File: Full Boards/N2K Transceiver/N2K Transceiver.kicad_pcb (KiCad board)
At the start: 4 copper layers, 80 x 60 mm, 75 parts, among them J1 JTAG, SW1 SW_MEC_5G, SW2 SW_MEC_5G, SW3 SW_MEC_5G

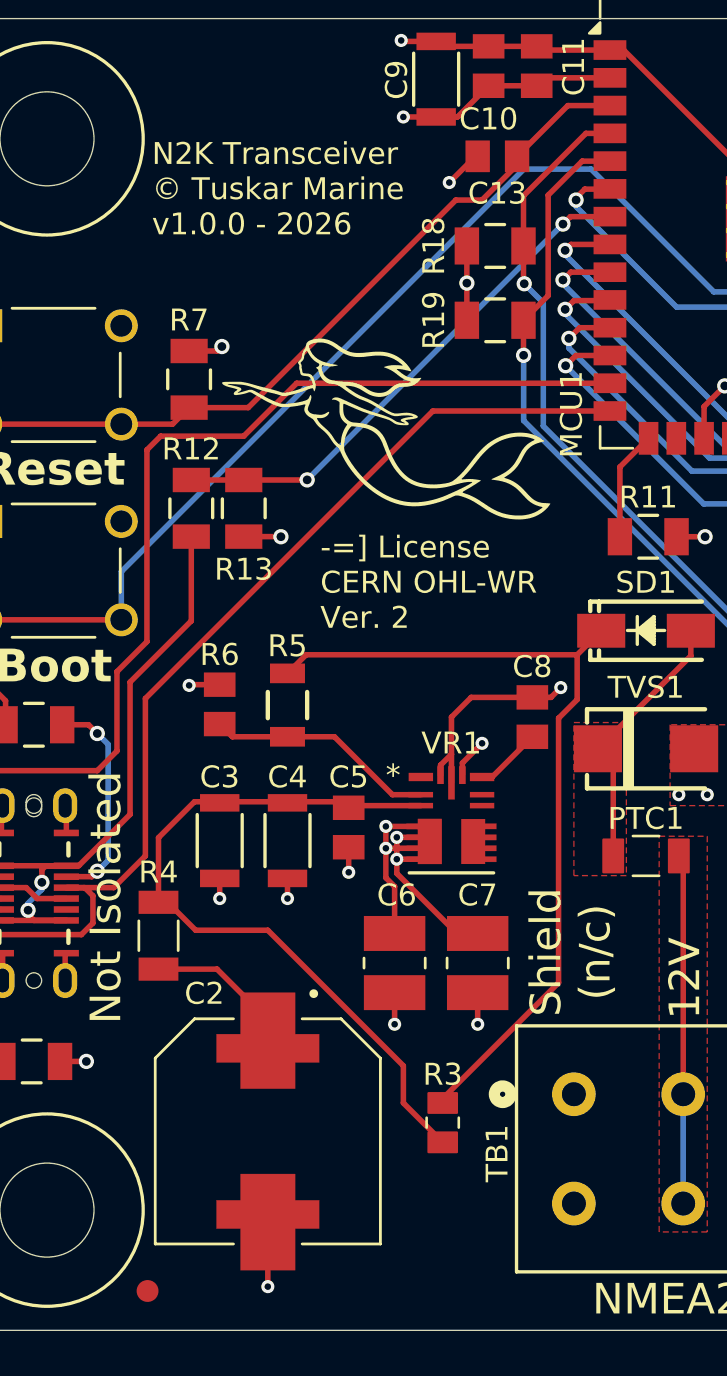
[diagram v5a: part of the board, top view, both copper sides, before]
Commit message: Removed the DNP'ed RC damper. With the TVS, it should not be possible for ringing to raise the voltage above 40v.
Signed-off-by: digimer <digital.mermaid@gmail.com>
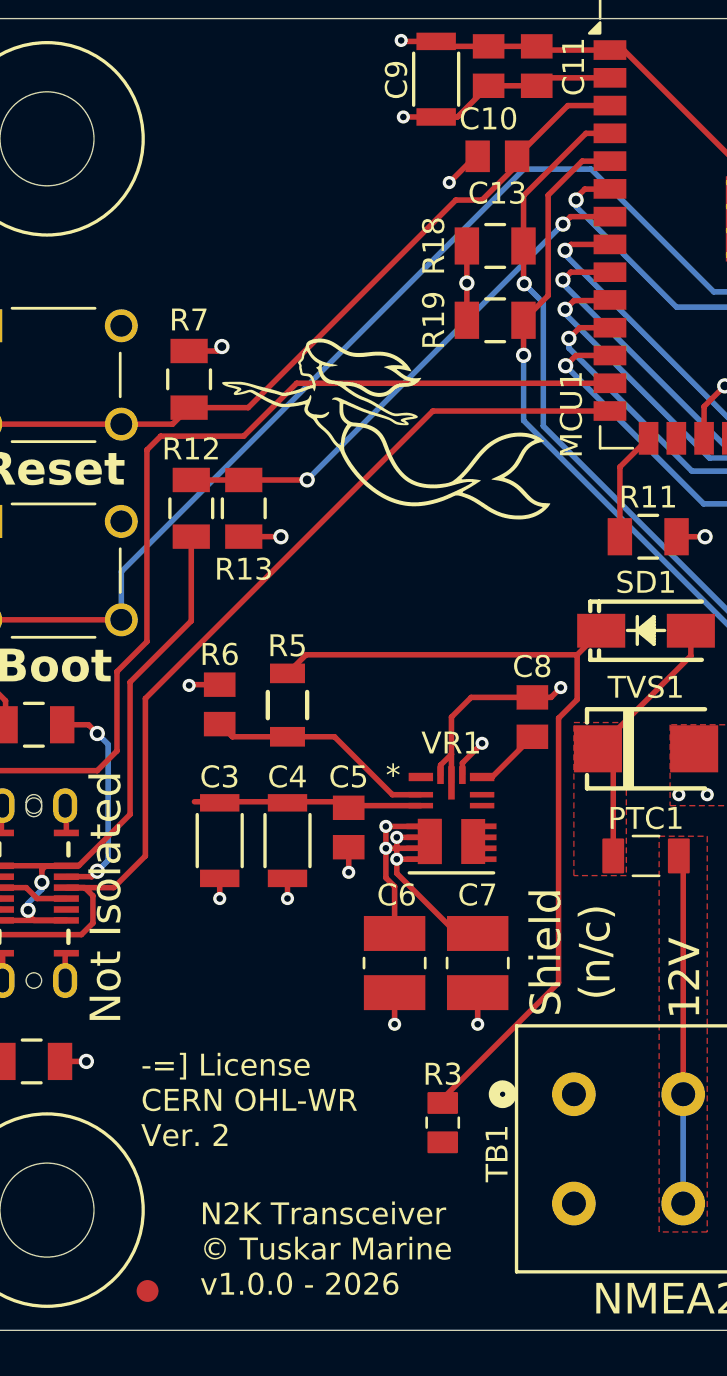
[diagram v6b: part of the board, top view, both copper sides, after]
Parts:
- removed C2: 330uF, mr-stuff:Panasonic EEH-ZU
- removed R4: 0.2R, mr-stuff:KOA SR73
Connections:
- C1 pad 2: GND -> +3.3V
- C10 pad 1: GND -> +3.3V
- C11 pad 1: GND -> +3.3V
- C14 pad 2: GND -> +3.3V
- C15 pad 2: GND -> +3.3V
- C6 pad 1: GND -> +3.3V
- C7 pad 1: GND -> +3.3V
- C9 pad 2: GND -> +3.3V
- CAN1 pad 3: GND -> +3.3V
- MCU1 pad 2: GND -> +3.3V
- R1 pad 2: GND -> +3.3V
- R16 pad 1: GND -> +3.3V
- R17 pad 1: GND -> +3.3V
- R18 pad 2: GND -> +3.3V
- R19 pad 2: GND -> +3.3V
- R23 pad 2: GND -> +3.3V
- R7 pad 2: GND -> +3.3V
- R8 pad 2: GND -> +3.3V
- ROM1 pad 1: GND -> +3.3V
- ROM1 pad 3: GND -> +3.3V
- ROM1 pad 8: GND -> +3.3V
- ROM2 pad 1: GND -> +3.3V
- ROM2 pad 2: GND -> +3.3V
- ROM2 pad 3: GND -> +3.3V
- ROM2 pad 8: GND -> +3.3V
- VR1 pad 4: GND -> +3.3V
- VR1 pad 9: GND -> +3.3V
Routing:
- net GND: track 214.5 -> 132.6 mm, vias 49 -> 32
- net +3.3V: track 0.00 -> 78.5 mm, vias 0 -> 16
- net Net-(VR1-VIN): track 33.5 -> 10.1 mm
- net Net-(C2-Pad1): track 7.26 -> 0.00 mm

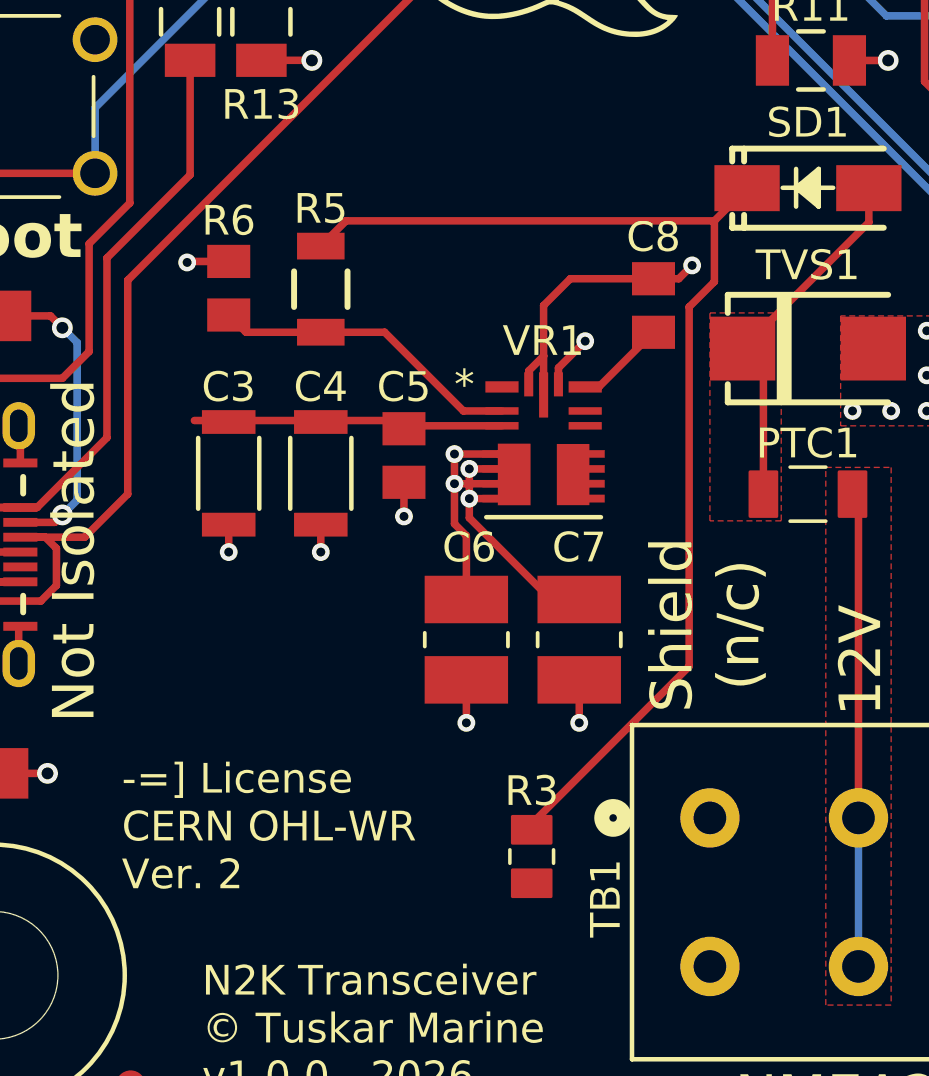
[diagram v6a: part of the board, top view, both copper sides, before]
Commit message: Resolved DRC issues.
Signed-off-by: digimer <digital.mermaid@gmail.com>
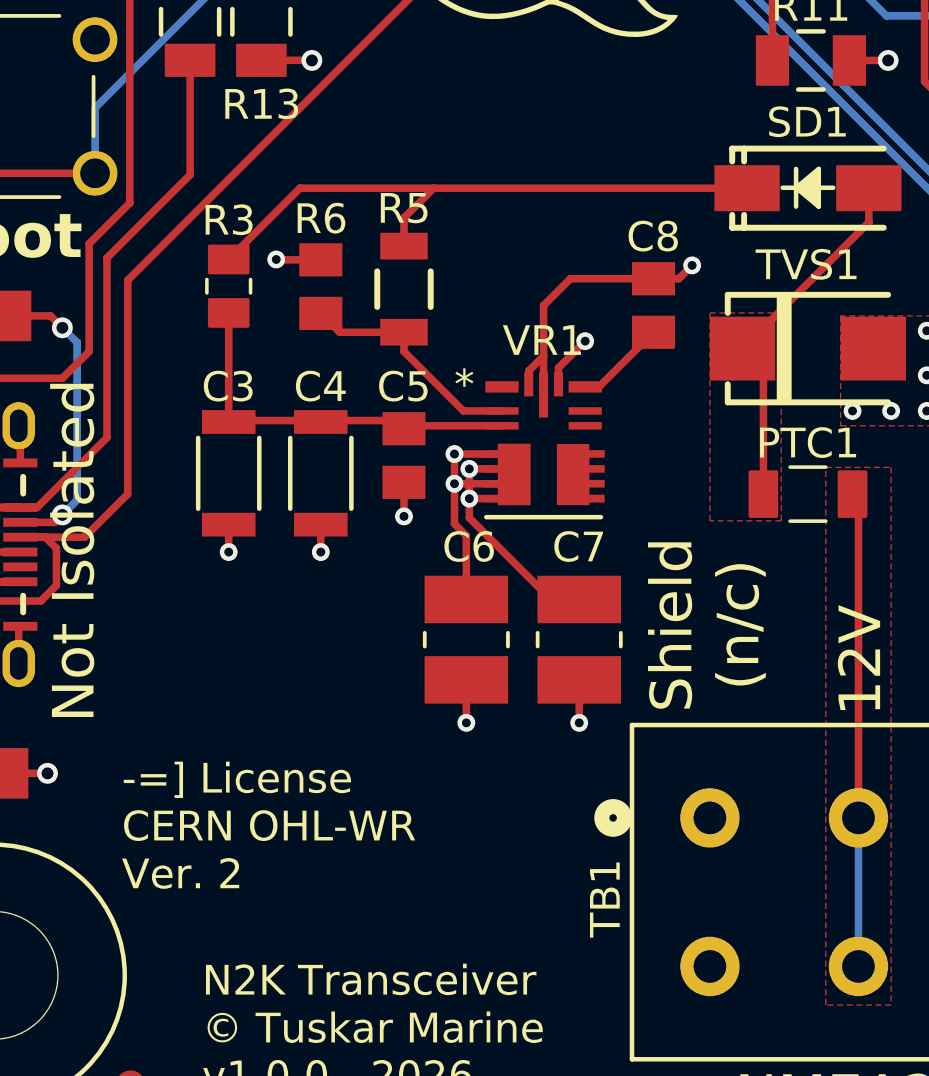
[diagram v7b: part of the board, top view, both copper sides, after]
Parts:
- moved R3 21.7 mm to (73.4, 74.6)
- moved R6 3.10 mm to (76.5, 74.6)
- moved R5 2.80 mm to (79.3, 74.7)
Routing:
- net V_RAW: track 38.0 -> 20.8 mm
- net Net-(VR1-EN): track 10.5 -> 7.84 mm
- net Net-(VR1-VIN): track 10.1 -> 12.6 mm
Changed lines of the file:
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@@
 	(footprint "mr-stuff:Vishay RCA-SR e3"
 		(layer "F.Cu")
-		(at 83.6 93.8 -90)
+		(at 73.4 74.6 -90)
 		(descr "Resistor SMD 0805")
 		(tags "resistor")
 		(property "Reference" "R3"
-			(at -2.2 0 180)
+			(at -2.2 0 0)
 			(layer "F.SilkS")
 			(effects
@@
 	(footprint "mr-stuff:Wurth WRIS-RSKS"
 		(layer "F.Cu")
-		(at 76.5 74.7 90)
+		(at 79.3 74.7 90)
 		(property "Reference" "R5"
 			(at 2.7 0 180)
@@
 	(footprint "mr-stuff:Stackpole RMCA0805"
 		(layer "F.Cu")
-		(at 73.4 74.6537 90)
+		(at 76.5 74.6 90)
 		(property "Reference" "R6"
 			(at 2.2537 0 0)
@@
 			(polygon
 				(pts
-					(xy 72.7269 74.9603) (xy 72.7269 74.3761) (xy 74.0731 74.3761) (xy 74.0731 74.9603)
+					(xy 75.8269 74.9066) (xy 75.8269 74.3224) (xy 77.1731 74.3224) (xy 77.1731 74.9066)
 				)
 			)
@@
 	)
 	(segment
-		(start 88.9 75.3)
-		(end 88.9 87.4)
-		(width 0.254)
-		(layer "F.Cu")
-		(net "V_RAW")
-	)
-	(segment
-		(start 89.75 72.4)
+		(start 80.3 71.3)
 		(end 90.85 71.3)
 		(width 0.254)
@@
 	)
 	(segment
-		(start 76.5 73.25)
-		(end 77.35 72.4)
-		(width 0.254)
-		(layer "F.Cu")
-		(net "V_RAW")
-	)
-	(segment
-		(start 89.75 72.4)
-		(end 89.75 74.45)
+		(start 79.3 73.25)
+		(end 79.3 72.3)
 		(width 0.254)
 		(layer "F.Cu")
@@
 	)
 	(segment
-		(start 77.35 72.4)
-		(end 89.75 72.4)
+		(start 73.4 73.7)
+		(end 75.8 71.3)
 		(width 0.254)
 		(layer "F.Cu")
@@
 	)
 	(segment
-		(start 89.75 74.45)
-		(end 88.9 75.3)
+		(start 79.3 72.3)
+		(end 80.3 71.3)
 		(width 0.254)
 		(layer "F.Cu")
@@
 	)
 	(segment
-		(start 88.9 87.4)
-		(end 83.6 92.7)
+		(start 75.8 71.3)
+		(end 80.3 71.3)
 		(width 0.254)
 		(layer "F.Cu")
@@
 	)
 	(segment
-		(start 72.2443 79.122)
-		(end 73.4 79.122)
+		(start 76.5 79.122)
+		(end 79.0737 79.122)
 		(width 0.254)
 		(layer "F.Cu")
@@
 	)
 	(segment
-		(start 76.5 79.122)
-		(end 79.0737 79.122)
+		(start 73.4 79.172)
+		(end 73.4 75.5)
 		(width 0.254)
 		(layer "F.Cu")
@@
 	)
 	(segment
-		(start 72.0335 73.7665)
-		(end 72 73.8)
-		(width 0.254)
-		(layer "F.Cu")
-		(net "GND")
-	)
-	(segment
 		(start 66.33 87.3)
 		(end 66.33 86.105)
@@
 	)
 	(segment
-		(start 81.744 44.344)
-		(end 81.7 44.3)
+		(start 75.0128 73.7128)
+		(end 75 73.7)
 		(width 0.254)
 		(layer "F.Cu")
@@
 	)
 	(segment
-		(start 73.4 73.7665)
-		(end 72.0335 73.7665)
+		(start 81.744 44.344)
+		(end 81.7 44.3)
 		(width 0.254)
 		(layer "F.Cu")
@@
 	)
 	(segment
+		(start 76.5 73.7128)
+		(end 75.0128 73.7128)
+		(width 0.254)
+		(layer "F.Cu")
+		(net "GND")
+	)
+	(segment
 		(start 111.7 81.1)
 		(end 107 81.1)
@@
 	)
 	(via
+		(at 75 73.7)
+		(size 0.6)
+		(drill 0.3)
+		(layers "F.Cu" "B.Cu")
+		(net "GND")
+	)
+	(via
 		(at 76.5 83.55)
 		(size 0.6)
@@
 	)
 	(via
-		(at 72 73.8)
-		(size 0.6)
-		(drill 0.3)
-		(layers "F.Cu" "B.Cu")
-		(net "GND")
-	)
-	(via
 		(at 83.9 50.8)
 		(size 0.6)
@@
 	)
 	(segment
-		(start 73.4 75.5699)
-		(end 73.9801 76.15)
+		(start 79.3 76.8)
+		(end 79.3 76.15)
 		(width 0.254)
 		(layer "F.Cu")
@@
 	)
 	(segment
-		(start 76.5 76.15)
-		(end 78.65 76.15)
+		(start 81.3 78.8)
+		(end 79.3 76.8)
 		(width 0.254)
 		(layer "F.Cu")
@@
 	)
 	(segment
-		(start 78.65 76.15)
-		(end 81.3 78.8)
+		(start 77.1338 76.15)
+		(end 76.5 75.5162)
 		(width 0.254)
 		(layer "F.Cu")
@@
 	)
 	(segment
-		(start 81.3 78.8)
-		(end 82.599114 78.8)
+		(start 79.3 76.15)
+		(end 77.1338 76.15)
 		(width 0.254)
 		(layer "F.Cu")
@@
 	)
 	(segment
-		(start 73.9801 76.15)
-		(end 76.5 76.15)
+		(start 81.3 78.8)
+		(end 82.599114 78.8)
 		(width 0.254)
 		(layer "F.Cu")
